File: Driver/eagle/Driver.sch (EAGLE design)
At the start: 32 parts, among them U1 L6205PDES, X1 22-23-2021, X2 22-23-2021, X3 22-23-2021

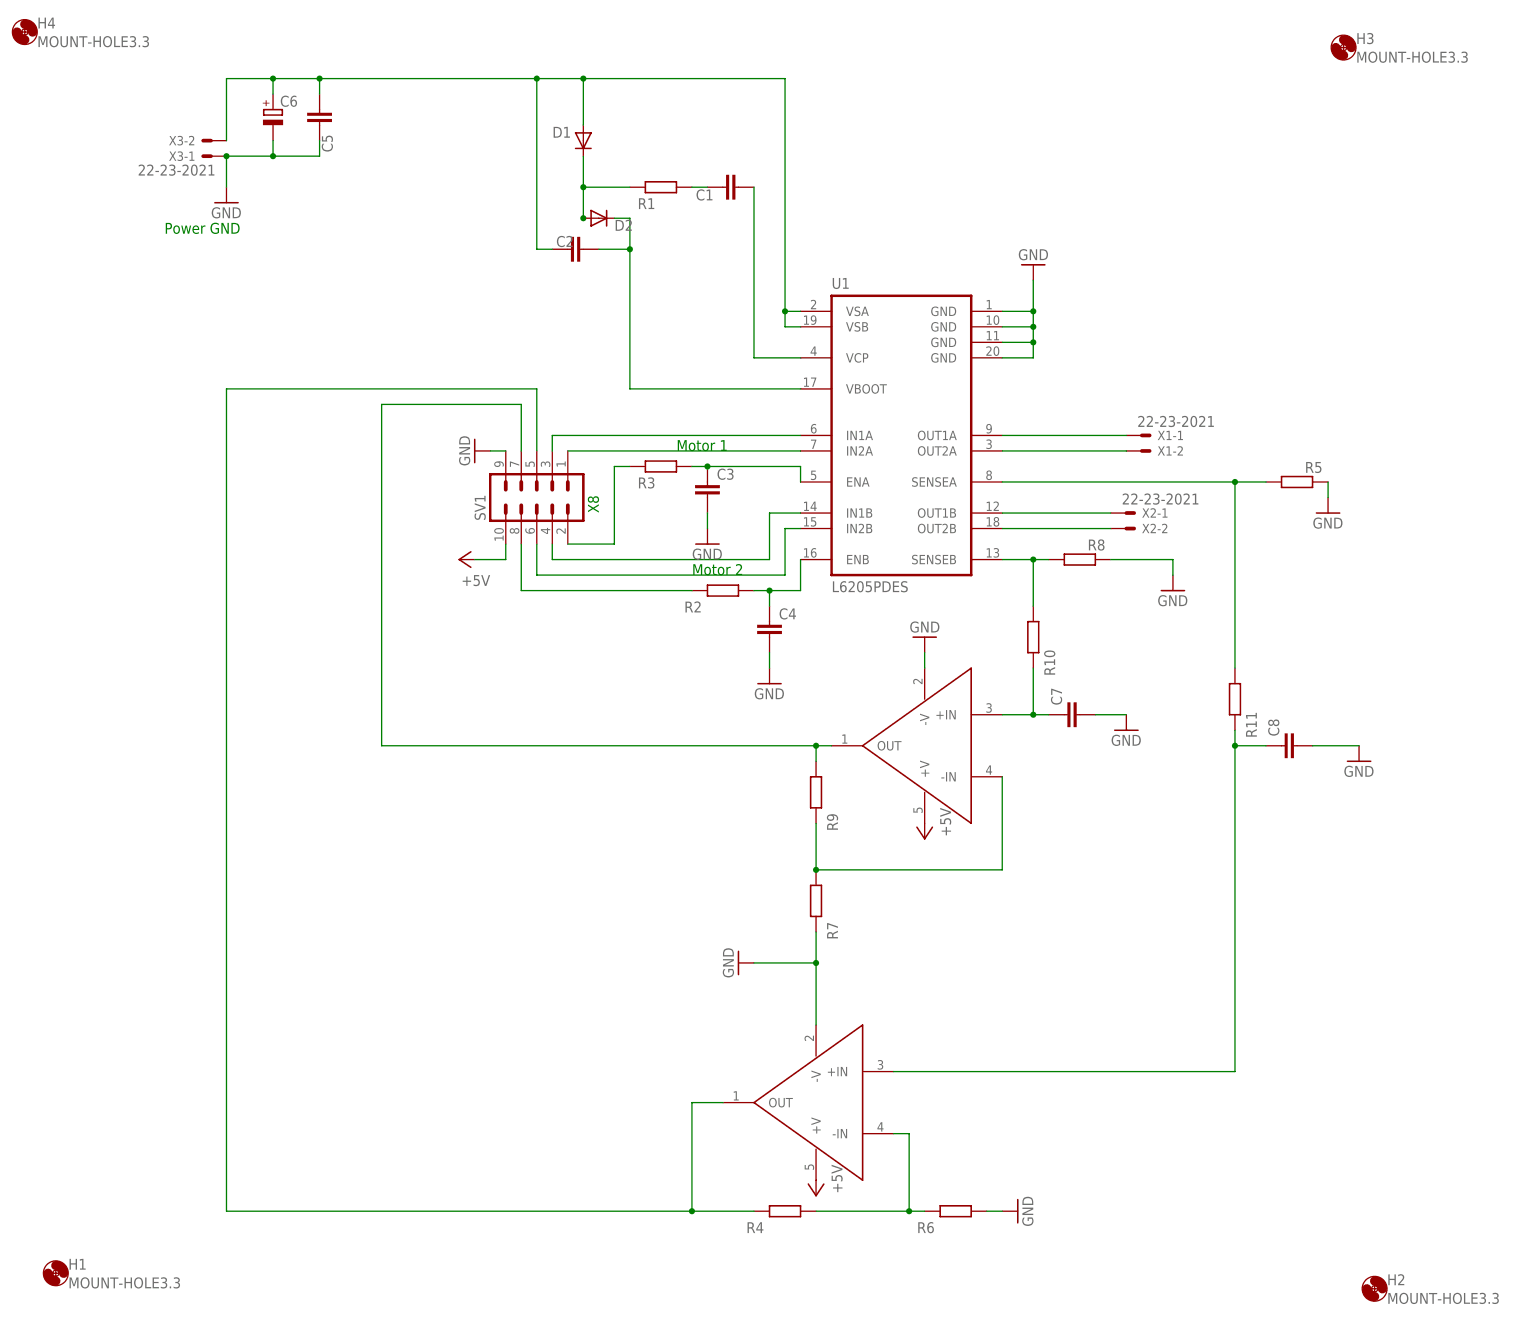
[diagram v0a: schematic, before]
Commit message: Updated driver schematic
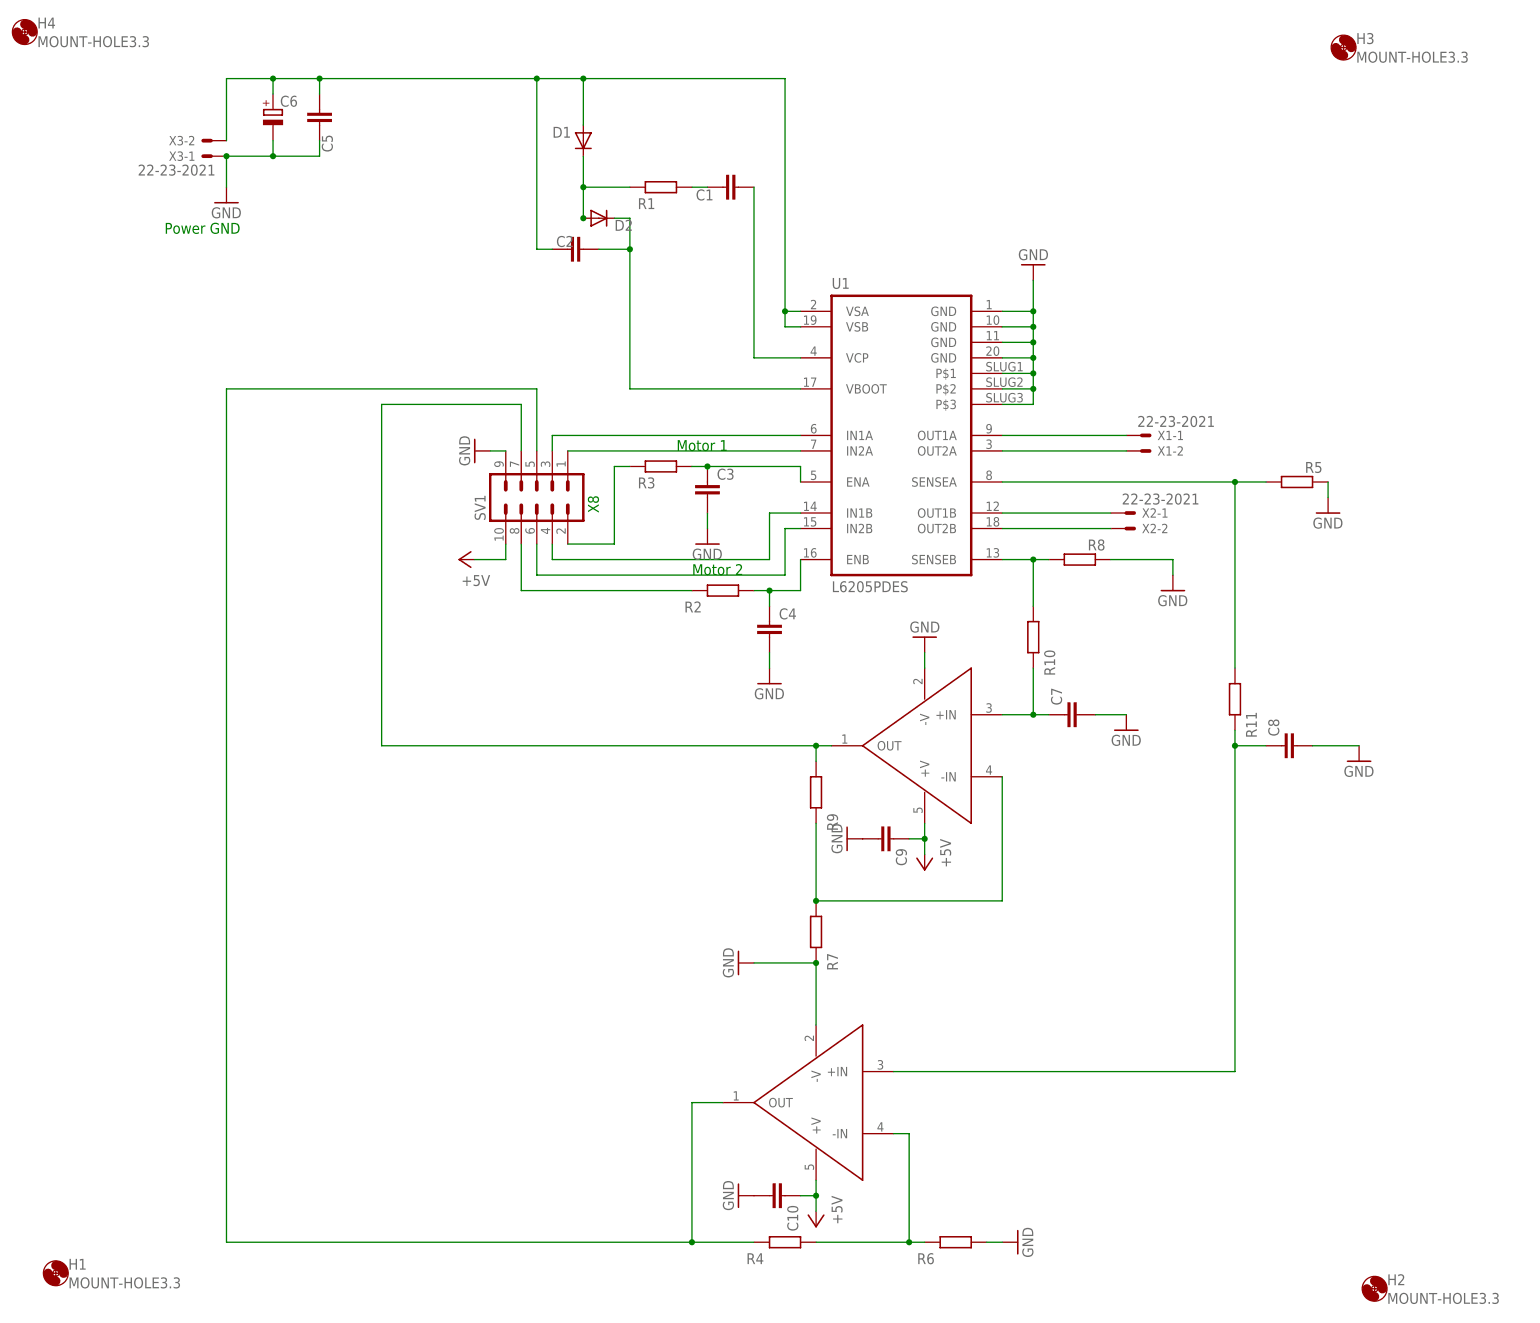
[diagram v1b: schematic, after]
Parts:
- added C10, C9: (no value), rcl:C-EUC0805
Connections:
- net +5V: now also C10.1, C9.1
- net GND: now also C10.2, C9.2, U1.P$1, U1.P$2, U1.P$3
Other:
- moved on the sheet: R4, R6, R7
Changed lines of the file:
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@@
 <part name="R11" library="rcl" deviceset="R-EU_" device="MELF0204W"/>
 <part name="R1" library="rcl" deviceset="R-EU_" device="MELF0204W"/>
+<part name="C9" library="rcl" deviceset="C-EU" device="C0805"/>
+<part name="C10" library="rcl" deviceset="C-EU" device="C0805"/>
+<part name="GND13" library="supply1" deviceset="GND" device=""/>
+<part name="GND14" library="supply1" deviceset="GND" device=""/>
 </parts>
 <sheets>
@@
 </instance>
 <instance part="U$2" gate="G$1" x="63.5" y="-50.8" rot="R180"/>
-<instance part="GND6" gate="1" x="88.9" y="-81.28" rot="R90"/>
+<instance part="GND6" gate="1" x="88.9" y="-86.36" rot="R90"/>
 <instance part="R8" gate="G$1" x="99.06" y="25.4" smashed="yes" rot="R180">
 <attribute name="NAME" x="100.33" y="26.8986" size="1.778" layer="95"/>
@@
 <instance part="U$3" gate="G$1" x="81.28" y="7.62" rot="R180"/>
 <instance part="GND10" gate="1" x="73.66" y="12.7" rot="R180"/>
-<instance part="P+1" gate="1" x="73.66" y="-20.32" rot="R180"/>
-<instance part="P+2" gate="1" x="55.88" y="-78.74" rot="R180"/>
+<instance part="P+1" gate="1" x="73.66" y="-25.4" rot="R180"/>
+<instance part="P+2" gate="1" x="55.88" y="-83.82" rot="R180"/>
 <instance part="P+3" gate="1" x="-2.54" y="25.4" rot="R90"/>
 <instance part="GND7" gate="1" x="43.18" y="-40.64" rot="R270"/>
@@
 <instance part="X3" gate="-1" x="-43.18" y="91.44" rot="R180"/>
 <instance part="X3" gate="-2" x="-43.18" y="93.98" rot="R180"/>
-<instance part="R4" gate="G$1" x="50.8" y="-81.28" smashed="yes">
-<attribute name="NAME" x="44.45" y="-84.8614" size="1.778" layer="95"/>
-<attribute name="VALUE" x="46.99" y="-84.582" size="1.778" layer="96"/>
-</instance>
-<instance part="R6" gate="G$1" x="78.74" y="-81.28" smashed="yes">
-<attribute name="NAME" x="72.39" y="-84.8614" size="1.778" layer="95"/>
-<attribute name="VALUE" x="74.93" y="-84.582" size="1.778" layer="96"/>
-</instance>
-<instance part="R7" gate="G$1" x="55.88" y="-30.48" smashed="yes" rot="R90">
-<attribute name="NAME" x="59.4614" y="-36.83" size="1.778" layer="95" rot="R90"/>
-<attribute name="VALUE" x="59.182" y="-34.29" size="1.778" layer="96" rot="R90"/>
+<instance part="R4" gate="G$1" x="50.8" y="-86.36" smashed="yes">
+<attribute name="NAME" x="44.45" y="-89.9414" size="1.778" layer="95"/>
+<attribute name="VALUE" x="46.99" y="-89.662" size="1.778" layer="96"/>
+</instance>
+<instance part="R6" gate="G$1" x="78.74" y="-86.36" smashed="yes">
+<attribute name="NAME" x="72.39" y="-89.9414" size="1.778" layer="95"/>
+<attribute name="VALUE" x="74.93" y="-89.662" size="1.778" layer="96"/>
+</instance>
+<instance part="R7" gate="G$1" x="55.88" y="-35.56" smashed="yes" rot="R90">
+<attribute name="NAME" x="59.4614" y="-41.91" size="1.778" layer="95" rot="R90"/>
+<attribute name="VALUE" x="59.182" y="-39.37" size="1.778" layer="96" rot="R90"/>
 </instance>
 <instance part="R9" gate="G$1" x="55.88" y="-12.7" smashed="yes" rot="R90">
@@
 <attribute name="VALUE" x="26.67" y="83.058" size="1.778" layer="96"/>
 </instance>
+<instance part="C9" gate="G$1" x="68.58" y="-20.32" rot="R270"/>
+<instance part="C10" gate="G$1" x="50.8" y="-78.74" rot="R270"/>
+<instance part="GND13" gate="1" x="43.18" y="-78.74" rot="R270"/>
+<instance part="GND14" gate="1" x="60.96" y="-20.32" rot="R270"/>
 </instances>
 <busses>
@@
 <junction x="91.44" y="63.5"/>
 <junction x="91.44" y="60.96"/>
-</segment>
-<segment>
-<wire x1="83.82" y1="-81.28" x2="86.36" y2="-81.28" width="0.1524" layer="91"/>
+<pinref part="U1" gate="G$1" pin="P$3"/>
+<wire x1="86.36" y1="50.8" x2="91.44" y2="50.8" width="0.1524" layer="91"/>
+<wire x1="91.44" y1="50.8" x2="91.44" y2="53.34" width="0.1524" layer="91"/>
+<pinref part="U1" gate="G$1" pin="P$2"/>
+<wire x1="91.44" y1="53.34" x2="91.44" y2="55.88" width="0.1524" layer="91"/>
+<wire x1="91.44" y1="55.88" x2="91.44" y2="58.42" width="0.1524" layer="91"/>
+<wire x1="86.36" y1="53.34" x2="91.44" y2="53.34" width="0.1524" layer="91"/>
+<pinref part="U1" gate="G$1" pin="P$1"/>
+<wire x1="86.36" y1="55.88" x2="91.44" y2="55.88" width="0.1524" layer="91"/>
+<junction x="91.44" y="58.42"/>
+<junction x="91.44" y="55.88"/>
+<junction x="91.44" y="53.34"/>
+</segment>
+<segment>
+<wire x1="83.82" y1="-86.36" x2="86.36" y2="-86.36" width="0.1524" layer="91"/>
 <pinref part="GND6" gate="1" pin="GND"/>
 <pinref part="R6" gate="G$1" pin="2"/>
@@
 <wire x1="55.88" y1="-50.8" x2="55.88" y2="-40.64" width="0.1524" layer="91"/>
 <pinref part="GND7" gate="1" pin="GND"/>
-<wire x1="55.88" y1="-40.64" x2="55.88" y2="-35.56" width="0.1524" layer="91"/>
 <wire x1="45.72" y1="-40.64" x2="55.88" y2="-40.64" width="0.1524" layer="91"/>
 <junction x="55.88" y="-40.64"/>
@@
 <pinref part="GND11" gate="1" pin="GND"/>
 <wire x1="137.16" y1="-5.08" x2="144.78" y2="-5.08" width="0.1524" layer="91"/>
+</segment>
+<segment>
+<pinref part="C10" gate="G$1" pin="2"/>
+<pinref part="GND13" gate="1" pin="GND"/>
+</segment>
+<segment>
+<pinref part="C9" gate="G$1" pin="2"/>
+<pinref part="GND14" gate="1" pin="GND"/>
 </segment>
 </net>
@@
 <net name="N$17" class="0">
 <segment>
-<wire x1="-40.64" y1="-81.28" x2="-40.64" y2="53.34" width="0.1524" layer="91"/>
+<wire x1="-40.64" y1="-86.36" x2="-40.64" y2="53.34" width="0.1524" layer="91"/>
 <wire x1="-40.64" y1="53.34" x2="10.16" y2="53.34" width="0.1524" layer="91"/>
 <pinref part="SV1" gate="G$1" pin="5"/>
 <wire x1="10.16" y1="53.34" x2="10.16" y2="43.18" width="0.1524" layer="91"/>
-<wire x1="45.72" y1="-81.28" x2="35.56" y2="-81.28" width="0.1524" layer="91"/>
+<wire x1="45.72" y1="-86.36" x2="35.56" y2="-86.36" width="0.1524" layer="91"/>
 <pinref part="U$2" gate="G$1" pin="OUT"/>
 <wire x1="40.64" y1="-63.5" x2="35.56" y2="-63.5" width="0.1524" layer="91"/>
-<wire x1="35.56" y1="-63.5" x2="35.56" y2="-81.28" width="0.1524" layer="91"/>
-<wire x1="35.56" y1="-81.28" x2="-40.64" y2="-81.28" width="0.1524" layer="91"/>
-<junction x="35.56" y="-81.28"/>
+<wire x1="35.56" y1="-63.5" x2="35.56" y2="-86.36" width="0.1524" layer="91"/>
+<wire x1="35.56" y1="-86.36" x2="-40.64" y2="-86.36" width="0.1524" layer="91"/>
+<junction x="35.56" y="-86.36"/>
 <pinref part="R4" gate="G$1" pin="1"/>
 </segment>
@@
 <segment>
 <pinref part="U$3" gate="G$1" pin="-IN"/>
-<wire x1="86.36" y1="-10.16" x2="86.36" y2="-25.4" width="0.1524" layer="91"/>
-<wire x1="86.36" y1="-25.4" x2="55.88" y2="-25.4" width="0.1524" layer="91"/>
-<wire x1="55.88" y1="-17.78" x2="55.88" y2="-25.4" width="0.1524" layer="91"/>
+<wire x1="86.36" y1="-10.16" x2="86.36" y2="-30.48" width="0.1524" layer="91"/>
+<wire x1="86.36" y1="-30.48" x2="55.88" y2="-30.48" width="0.1524" layer="91"/>
+<wire x1="55.88" y1="-17.78" x2="55.88" y2="-30.48" width="0.1524" layer="91"/>
 <pinref part="R7" gate="G$1" pin="2"/>
-<junction x="55.88" y="-25.4"/>
+<junction x="55.88" y="-30.48"/>
 <pinref part="R9" gate="G$1" pin="1"/>
 </segment>
@@
 <pinref part="U$2" gate="G$1" pin="-IN"/>
 <wire x1="68.58" y1="-68.58" x2="71.12" y2="-68.58" width="0.1524" layer="91"/>
-<wire x1="55.88" y1="-81.28" x2="71.12" y2="-81.28" width="0.1524" layer="91"/>
-<wire x1="71.12" y1="-81.28" x2="73.66" y2="-81.28" width="0.1524" layer="91"/>
-<wire x1="71.12" y1="-68.58" x2="71.12" y2="-81.28" width="0.1524" layer="91"/>
-<junction x="71.12" y="-81.28"/>
+<wire x1="55.88" y1="-86.36" x2="71.12" y2="-86.36" width="0.1524" layer="91"/>
+<wire x1="71.12" y1="-86.36" x2="73.66" y2="-86.36" width="0.1524" layer="91"/>
+<wire x1="71.12" y1="-68.58" x2="71.12" y2="-86.36" width="0.1524" layer="91"/>
+<junction x="71.12" y="-86.36"/>
 <pinref part="R4" gate="G$1" pin="2"/>
 <pinref part="R6" gate="G$1" pin="1"/>
@@
 <pinref part="U$2" gate="G$1" pin="+V"/>
 <pinref part="P+2" gate="1" pin="+5V"/>
+<wire x1="55.88" y1="-81.28" x2="55.88" y2="-78.74" width="0.1524" layer="91"/>
+<pinref part="C10" gate="G$1" pin="1"/>
+<wire x1="55.88" y1="-78.74" x2="55.88" y2="-76.2" width="0.1524" layer="91"/>
+<wire x1="53.34" y1="-78.74" x2="55.88" y2="-78.74" width="0.1524" layer="91"/>
+<junction x="55.88" y="-78.74"/>
 </segment>
 <segment>
 <pinref part="U$3" gate="G$1" pin="+V"/>
 <pinref part="P+1" gate="1" pin="+5V"/>
-</segment>
-<segment>
+<wire x1="73.66" y1="-22.86" x2="73.66" y2="-20.32" width="0.1524" layer="91"/>
+<pinref part="C9" gate="G$1" pin="1"/>
+<wire x1="73.66" y1="-20.32" x2="73.66" y2="-17.78" width="0.1524" layer="91"/>
+<wire x1="71.12" y1="-20.32" x2="73.66" y2="-20.32" width="0.1524" layer="91"/>
+<junction x="73.66" y="-20.32"/>
+</segment>
+<segment>
